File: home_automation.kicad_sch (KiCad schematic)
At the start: 44 parts

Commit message: Anotate the Components
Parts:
- gave numbers to parts that had none: 44

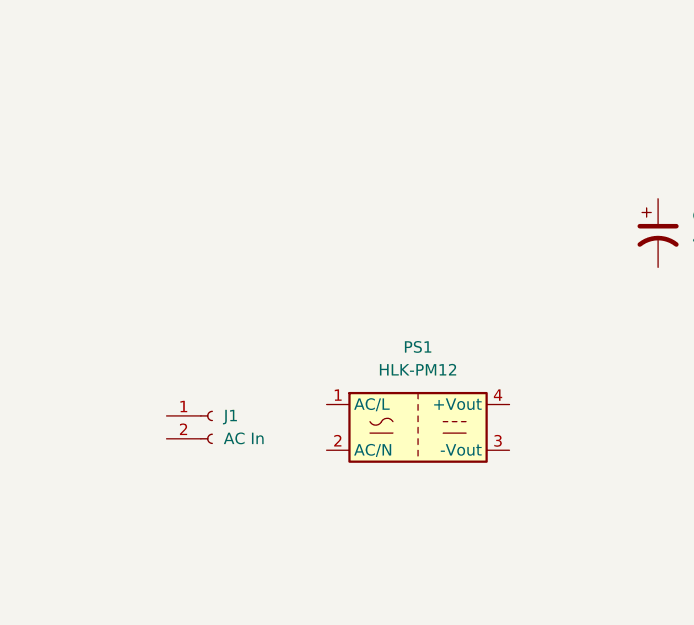
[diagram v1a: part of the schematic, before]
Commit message: Power section Wiring Completed
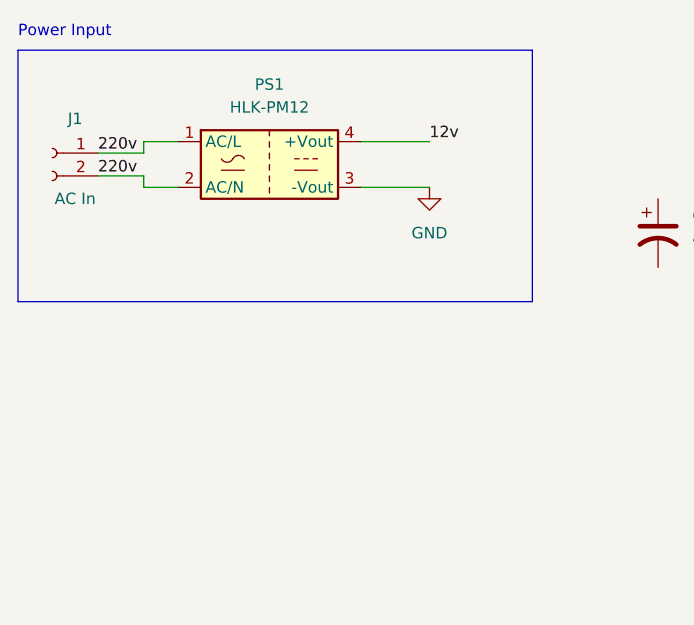
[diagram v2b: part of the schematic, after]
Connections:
- net 220v: now reaches J1.1 (Pin_1)
- net 220v: now also J1.2 (Pin_2), PS1.1 (AC/L), PS1.2 (AC/N)
- net GND: now reaches PS1.3 (-Vout)
- net 12v: now reaches PS1.4 (+Vout)
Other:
- note added: "Power Input"
- moved on the sheet: J1, PS1
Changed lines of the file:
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@@
     (rev "v1")
+  )
+  (wire (pts (xy 34.29 29.21) (xy 39.37 29.21))
+    (stroke (width 0) (type default) (color 0 0 0 0))
+  )
+  (wire (pts (xy 39.37 27.94) (xy 43.18 27.94))
+    (stroke (width 0) (type default) (color 0 0 0 0))
+  )
+  (wire (pts (xy 39.37 31.75) (xy 39.37 33.02))
+    (stroke (width 0) (type default) (color 0 0 0 0))
+  )
+  (polyline (pts (xy 25.4 17.78) (xy 82.55 17.78))
+    (stroke (width 0) (type default) (color 0 0 0 0))
+  )
+  (wire (pts (xy 63.5 33.02) (xy 71.12 33.02))
+    (stroke (width 0) (type default) (color 0 0 0 0))
+  )
+  (wire (pts (xy 63.5 27.94) (xy 71.12 27.94))
+    (stroke (width 0) (type default) (color 0 0 0 0))
+  )
+  (polyline (pts (xy 25.4 17.78) (xy 25.4 45.72))
+    (stroke (width 0) (type default) (color 0 0 0 0))
+  )
+  (polyline (pts (xy 82.55 45.72) (xy 25.4 45.72))
+    (stroke (width 0) (type default) (color 0 0 0 0))
+  )
+  (wire (pts (xy 34.29 31.75) (xy 39.37 31.75))
+    (stroke (width 0) (type default) (color 0 0 0 0))
+  )
+  (polyline (pts (xy 82.55 17.78) (xy 82.55 45.72))
+    (stroke (width 0) (type default) (color 0 0 0 0))
+  )
+  (wire (pts (xy 39.37 33.02) (xy 43.18 33.02))
+    (stroke (width 0) (type default) (color 0 0 0 0))
+  )
+  (wire (pts (xy 39.37 29.21) (xy 39.37 27.94))
+    (stroke (width 0) (type default) (color 0 0 0 0))
+  )
+  (text "Power Input\n" (at 25.4 16.51 0)
+    (effects (font (size 1.27 1.27)) (justify left bottom))
+  )
+  (label "12v" (at 71.12 27.94 0)
+    (effects (font (size 1.27 1.27)) (justify left bottom))
+  )
+  (label "220v" (at 34.29 29.21 0)
+    (effects (font (size 1.27 1.27)) (justify left bottom))
+  )
+  (label "220v" (at 34.29 31.75 0)
+    (effects (font (size 1.27 1.27)) (justify left bottom))
   )
   (symbol (lib_id "Transistor_CUSTOM:D882_NPN_transistor") (at 245.11 149.86 0) (unit 1)
@@
     (pin "2")
   )
+  (symbol (lib_id "power:GND") (at 71.12 33.02 0) (unit 1)
+    (in_bom yes) (on_board yes) (fields_autoplaced)
+    (property "Reference" "#PWR?" (id 0) (at 71.12 39.37 0)
+      (effects (font (size 1.27 1.27)) hide)
+    )
+    (property "Value" "GND" (id 1) (at 71.12 38.1 0))
+    (property "Footprint" "" (id 2) (at 71.12 33.02 0)
+      (effects (font (size 1.27 1.27)) hide)
+    )
+    (property "Datasheet" "" (id 3) (at 71.12 33.02 0)
+      (effects (font (size 1.27 1.27)) hide)
+    )
+    (pin "1")
+  )
   (symbol (lib_id "Relay_SPDT:Relay_SPDT") (at 127 142.24 0) (unit 1)
     (in_bom yes) (on_board yes) (fields_autoplaced)
@@
     (pin "4")
   )
-  (symbol (lib_id "Connector:Conn_01x02_Female") (at 46.99 58.42 0) (unit 1)
-    (in_bom yes) (on_board yes) (fields_autoplaced)
-    (property "Reference" "J1" (id 0) (at 48.26 58.4199 0)
-      (effects (font (size 1.27 1.27)) (justify left))
-    )
-    (property "Value" "AC In" (id 1) (at 48.26 60.9599 0)
-      (effects (font (size 1.27 1.27)) (justify left))
-    )
-    (property "Footprint" "" (id 2) (at 46.99 58.42 0)
-      (effects (font (size 1.27 1.27)) hide)
-    )
-    (property "Datasheet" "~" (id 3) (at 46.99 58.42 0)
+  (symbol (lib_id "Connector:Conn_01x02_Female") (at 29.21 29.21 0) (mirror y) (unit 1)
+    (in_bom yes) (on_board yes)
+    (property "Reference" "J1" (id 0) (at 31.75 25.4 0))
+    (property "Value" "AC In" (id 1) (at 31.75 34.29 0))
+    (property "Footprint" "" (id 2) (at 29.21 29.21 0)
+      (effects (font (size 1.27 1.27)) hide)
+    )
+    (property "Datasheet" "~" (id 3) (at 29.21 29.21 0)
       (effects (font (size 1.27 1.27)) hide)
     )
@@
     (pin "2")
   )
-  (symbol (lib_id "Converter_ACDC:HLK-PM12") (at 69.85 59.69 0) (unit 1)
-    (in_bom yes) (on_board yes) (fields_autoplaced)
-    (property "Reference" "PS1" (id 0) (at 69.85 50.8 0))
-    (property "Value" "HLK-PM12" (id 1) (at 69.85 53.34 0))
-    (property "Footprint" "Converter_ACDC:Converter_ACDC_HiLink_HLK-PMxx" (id 2) (at 69.85 67.31 0)
-      (effects (font (size 1.27 1.27)) hide)
-    )
-    (property "Datasheet" "http://www.hlktech.net/product_detail.php?ProId=56" (id 3) (at 80.01 68.58 0)
+  (symbol (lib_id "Converter_ACDC:HLK-PM12") (at 53.34 30.48 0) (unit 1)
+    (in_bom yes) (on_board yes) (fields_autoplaced)
+    (property "Reference" "PS1" (id 0) (at 53.34 21.59 0))
+    (property "Value" "HLK-PM12" (id 1) (at 53.34 24.13 0))
+    (property "Footprint" "Converter_ACDC:Converter_ACDC_HiLink_HLK-PMxx" (id 2) (at 53.34 38.1 0)
+      (effects (font (size 1.27 1.27)) hide)
+    )
+    (property "Datasheet" "http://www.hlktech.net/product_detail.php?ProId=56" (id 3) (at 63.5 39.37 0)
       (effects (font (size 1.27 1.27)) hide)
     )
@@
   )
   (symbol_instances
+    (path "/2accfbf2-56a4-48cd-9686-a76d5e02c6cd"
+      (reference "#PWR?") (unit 1) (value "GND") (footprint "")
+    )
     (path "/6bde53ab-782b-4476-8581-8063e3f079ec"
       (reference "C1") (unit 1) (value "470uF") (footprint "")

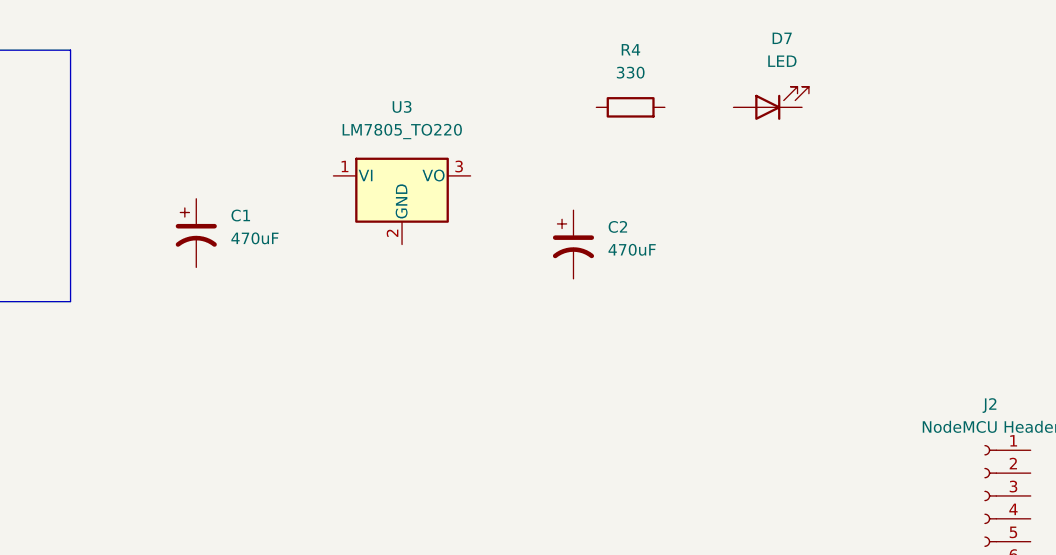
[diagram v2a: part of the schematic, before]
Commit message: 12v to 5v  Wiring Completed
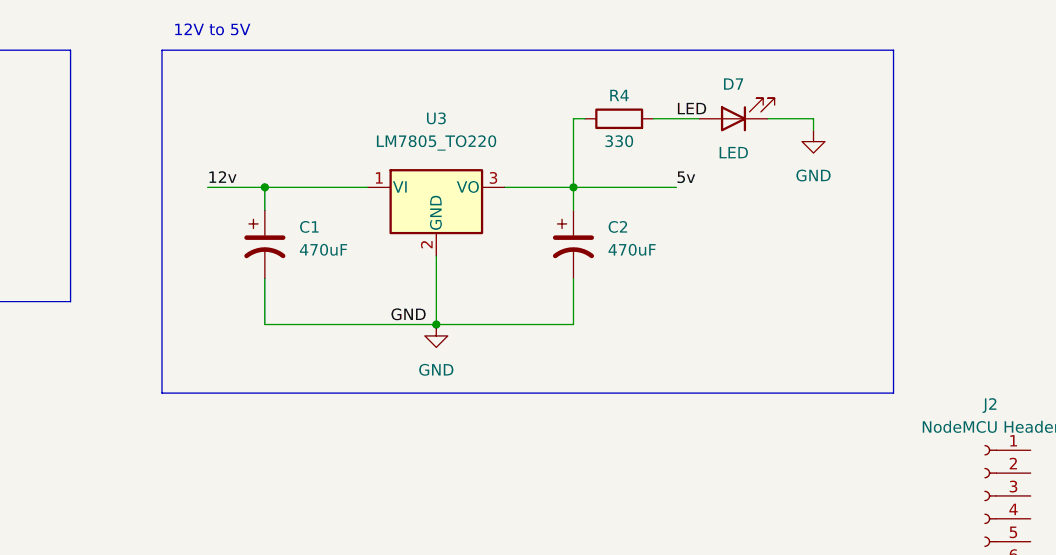
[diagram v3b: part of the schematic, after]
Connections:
- net 12v: now also C1.1, U3.1 (VI)
- net GND: now also C1.2, C2.2, D7.1 (K), U3.2 (GND)
- net 5v: now reaches C2.1
- net 5v: now also R4.1, U3.3 (VO)
- net LED: now reaches D7.2 (A)
- net LED: now also R4.2
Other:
- note added: "12V to 5V"
- moved on the sheet: C1, D7, R4, U3
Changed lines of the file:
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@@
     (rev "v1")
   )
+  (junction (at 104.14 33.02) (diameter 0) (color 0 0 0 0)
+  )
+  (junction (at 138.43 33.02) (diameter 0) (color 0 0 0 0)
+  )
+  (junction (at 123.19 48.26) (diameter 0) (color 0 0 0 0)
+  )
+  (wire (pts (xy 123.19 48.26) (xy 138.43 48.26))
+    (stroke (width 0) (type default) (color 0 0 0 0))
+  )
+  (wire (pts (xy 138.43 33.02) (xy 138.43 35.56))
+    (stroke (width 0) (type default) (color 0 0 0 0))
+  )
+  (wire (pts (xy 104.14 33.02) (xy 115.57 33.02))
+    (stroke (width 0) (type default) (color 0 0 0 0))
+  )
   (wire (pts (xy 34.29 29.21) (xy 39.37 29.21))
     (stroke (width 0) (type default) (color 0 0 0 0))
   )
+  (polyline (pts (xy 173.99 55.88) (xy 92.71 55.88))
+    (stroke (width 0) (type default) (color 0 0 0 0))
+  )
   (wire (pts (xy 39.37 27.94) (xy 43.18 27.94))
     (stroke (width 0) (type default) (color 0 0 0 0))
   )
+  (wire (pts (xy 147.32 25.4) (xy 152.4 25.4))
+    (stroke (width 0) (type default) (color 0 0 0 0))
+  )
+  (polyline (pts (xy 92.71 17.78) (xy 92.71 55.88))
+    (stroke (width 0) (type default) (color 0 0 0 0))
+  )
+  (wire (pts (xy 139.7 25.4) (xy 138.43 25.4))
+    (stroke (width 0) (type default) (color 0 0 0 0))
+  )
   (wire (pts (xy 39.37 31.75) (xy 39.37 33.02))
     (stroke (width 0) (type default) (color 0 0 0 0))
   )
+  (wire (pts (xy 130.81 33.02) (xy 138.43 33.02))
+    (stroke (width 0) (type default) (color 0 0 0 0))
+  )
+  (wire (pts (xy 138.43 25.4) (xy 138.43 33.02))
+    (stroke (width 0) (type default) (color 0 0 0 0))
+  )
+  (wire (pts (xy 123.19 40.64) (xy 123.19 48.26))
+    (stroke (width 0) (type default) (color 0 0 0 0))
+  )
+  (wire (pts (xy 138.43 33.02) (xy 149.86 33.02))
+    (stroke (width 0) (type default) (color 0 0 0 0))
+  )
   (polyline (pts (xy 25.4 17.78) (xy 82.55 17.78))
     (stroke (width 0) (type default) (color 0 0 0 0))
@@
     (stroke (width 0) (type default) (color 0 0 0 0))
   )
+  (wire (pts (xy 138.43 48.26) (xy 138.43 43.18))
+    (stroke (width 0) (type default) (color 0 0 0 0))
+  )
+  (wire (pts (xy 104.14 43.18) (xy 104.14 48.26))
+    (stroke (width 0) (type default) (color 0 0 0 0))
+  )
   (wire (pts (xy 63.5 27.94) (xy 71.12 27.94))
     (stroke (width 0) (type default) (color 0 0 0 0))
   )
+  (polyline (pts (xy 92.71 17.78) (xy 173.99 17.78))
+    (stroke (width 0) (type default) (color 0 0 0 0))
+  )
   (polyline (pts (xy 25.4 17.78) (xy 25.4 45.72))
     (stroke (width 0) (type default) (color 0 0 0 0))
   )
+  (wire (pts (xy 165.1 25.4) (xy 165.1 26.67))
+    (stroke (width 0) (type default) (color 0 0 0 0))
+  )
+  (wire (pts (xy 97.79 33.02) (xy 104.14 33.02))
+    (stroke (width 0) (type default) (color 0 0 0 0))
+  )
   (polyline (pts (xy 82.55 45.72) (xy 25.4 45.72))
     (stroke (width 0) (type default) (color 0 0 0 0))
@@
     (stroke (width 0) (type default) (color 0 0 0 0))
   )
+  (polyline (pts (xy 173.99 17.78) (xy 173.99 55.88))
+    (stroke (width 0) (type default) (color 0 0 0 0))
+  )
   (polyline (pts (xy 82.55 17.78) (xy 82.55 45.72))
     (stroke (width 0) (type default) (color 0 0 0 0))
   )
+  (wire (pts (xy 160.02 25.4) (xy 165.1 25.4))
+    (stroke (width 0) (type default) (color 0 0 0 0))
+  )
   (wire (pts (xy 39.37 33.02) (xy 43.18 33.02))
+    (stroke (width 0) (type default) (color 0 0 0 0))
+  )
+  (wire (pts (xy 104.14 33.02) (xy 104.14 35.56))
+    (stroke (width 0) (type default) (color 0 0 0 0))
+  )
+  (wire (pts (xy 104.14 48.26) (xy 123.19 48.26))
     (stroke (width 0) (type default) (color 0 0 0 0))
   )
@@
     (effects (font (size 1.27 1.27)) (justify left bottom))
   )
+  (text "12V to 5V\n" (at 93.98 16.51 0)
+    (effects (font (size 1.27 1.27)) (justify left bottom))
+  )
   (label "12v" (at 71.12 27.94 0)
     (effects (font (size 1.27 1.27)) (justify left bottom))
@@
     (effects (font (size 1.27 1.27)) (justify left bottom))
   )
+  (label "GND" (at 118.11 48.26 0)
+    (effects (font (size 1.27 1.27)) (justify left bottom))
+  )
   (label "220v" (at 34.29 31.75 0)
+    (effects (font (size 1.27 1.27)) (justify left bottom))
+  )
+  (label "5v" (at 149.86 33.02 0)
+    (effects (font (size 1.27 1.27)) (justify left bottom))
+  )
+  (label "LED" (at 149.86 25.4 0)
+    (effects (font (size 1.27 1.27)) (justify left bottom))
+  )
+  (label "12v" (at 97.79 33.02 0)
     (effects (font (size 1.27 1.27)) (justify left bottom))
   )
@@
     (pin "3")
   )
-  (symbol (lib_id "Regulator_Linear:LM7805_TO220") (at 119.38 31.75 0) (unit 1)
-    (in_bom yes) (on_board yes) (fields_autoplaced)
-    (property "Reference" "U3" (id 0) (at 119.38 24.13 0))
-    (property "Value" "LM7805_TO220" (id 1) (at 119.38 26.67 0))
-    (property "Footprint" "Package_TO_SOT_THT:TO-220-3_Vertical" (id 2) (at 119.38 26.035 0)
+  (symbol (lib_id "Regulator_Linear:LM7805_TO220") (at 123.19 33.02 0) (unit 1)
+    (in_bom yes) (on_board yes) (fields_autoplaced)
+    (property "Reference" "U3" (id 0) (at 123.19 25.4 0))
+    (property "Value" "LM7805_TO220" (id 1) (at 123.19 27.94 0))
+    (property "Footprint" "Package_TO_SOT_THT:TO-220-3_Vertical" (id 2) (at 123.19 27.305 0)
       (effects (font (size 1.27 1.27) italic) hide)
     )
-    (property "Datasheet" "https://www.onsemi.cn/PowerSolutions/document/MC7800-D.PDF" (id 3) (at 119.38 33.02 0)
+    (property "Datasheet" "https://www.onsemi.cn/PowerSolutions/document/MC7800-D.PDF" (id 3) (at 123.19 34.29 0)
       (effects (font (size 1.27 1.27)) hide)
     )
@@
     (pin "3")
     (pin "4")
+  )
+  (symbol (lib_id "power:GND") (at 123.19 48.26 0) (unit 1)
+    (in_bom yes) (on_board yes) (fields_autoplaced)
+    (property "Reference" "#PWR?" (id 0) (at 123.19 54.61 0)
+      (effects (font (size 1.27 1.27)) hide)
+    )
+    (property "Value" "GND" (id 1) (at 123.19 53.34 0))
+    (property "Footprint" "" (id 2) (at 123.19 48.26 0)
+      (effects (font (size 1.27 1.27)) hide)
+    )
+    (property "Datasheet" "" (id 3) (at 123.19 48.26 0)
+      (effects (font (size 1.27 1.27)) hide)
+    )
+    (pin "1")
   )
   (symbol (lib_id "Connector:Conn_01x02_Female") (at 29.21 29.21 0) (mirror y) (unit 1)
@@
     (pin "2")
   )
-  (symbol (lib_id "Device:LED") (at 160.02 24.13 180) (unit 1)
-    (in_bom yes) (on_board yes) (fields_autoplaced)
-    (property "Reference" "D7" (id 0) (at 161.6075 16.51 0))
-    (property "Value" "LED" (id 1) (at 161.6075 19.05 0))
-    (property "Footprint" "" (id 2) (at 160.02 24.13 0)
-      (effects (font (size 1.27 1.27)) hide)
-    )
-    (property "Datasheet" "~" (id 3) (at 160.02 24.13 0)
+  (symbol (lib_id "Device:LED") (at 156.21 25.4 180) (unit 1)
+    (in_bom yes) (on_board yes)
+    (property "Reference" "D7" (id 0) (at 156.21 21.59 0))
+    (property "Value" "LED" (id 1) (at 156.21 29.21 0))
+    (property "Footprint" "" (id 2) (at 156.21 25.4 0)
+      (effects (font (size 1.27 1.27)) hide)
+    )
+    (property "Datasheet" "~" (id 3) (at 156.21 25.4 0)
       (effects (font (size 1.27 1.27)) hide)
     )
@@
     (pin "3")
   )
-  (symbol (lib_id "Device:C_Polarized_US") (at 96.52 38.1 0) (unit 1)
-    (in_bom yes) (on_board yes) (fields_autoplaced)
-    (property "Reference" "C1" (id 0) (at 100.33 36.1949 0)
-      (effects (font (size 1.27 1.27)) (justify left))
-    )
-    (property "Value" "470uF" (id 1) (at 100.33 38.7349 0)
-      (effects (font (size 1.27 1.27)) (justify left))
-    )
-    (property "Footprint" "" (id 2) (at 96.52 38.1 0)
-      (effects (font (size 1.27 1.27)) hide)
-    )
-    (property "Datasheet" "~" (id 3) (at 96.52 38.1 0)
+  (symbol (lib_id "Device:C_Polarized_US") (at 104.14 39.37 0) (unit 1)
+    (in_bom yes) (on_board yes) (fields_autoplaced)
+    (property "Reference" "C1" (id 0) (at 107.95 37.4649 0)
+      (effects (font (size 1.27 1.27)) (justify left))
+    )
+    (property "Value" "470uF" (id 1) (at 107.95 40.0049 0)
+      (effects (font (size 1.27 1.27)) (justify left))
+    )
+    (property "Footprint" "" (id 2) (at 104.14 39.37 0)
+      (effects (font (size 1.27 1.27)) hide)
+    )
+    (property "Datasheet" "~" (id 3) (at 104.14 39.37 0)
       (effects (font (size 1.27 1.27)) hide)
     )
@@
     (pin "9")
   )
-  (symbol (lib_id "Device:R") (at 144.78 24.13 90) (unit 1)
-    (in_bom yes) (on_board yes) (fields_autoplaced)
-    (property "Reference" "R4" (id 0) (at 144.78 17.78 90))
-    (property "Value" "330" (id 1) (at 144.78 20.32 90))
-    (property "Footprint" "" (id 2) (at 144.78 25.908 90)
-      (effects (font (size 1.27 1.27)) hide)
-    )
-    (property "Datasheet" "~" (id 3) (at 144.78 24.13 0)
+  (symbol (lib_id "Device:R") (at 143.51 25.4 90) (unit 1)
+    (in_bom yes) (on_board yes)
+    (property "Reference" "R4" (id 0) (at 143.51 22.86 90))
+    (property "Value" "330" (id 1) (at 143.51 27.94 90))
+    (property "Footprint" "" (id 2) (at 143.51 27.178 90)
+      (effects (font (size 1.27 1.27)) hide)
+    )
+    (property "Datasheet" "~" (id 3) (at 143.51 25.4 0)
       (effects (font (size 1.27 1.27)) hide)
     )
@@
     (pin "1")
     (pin "2")
+  )
+  (symbol (lib_id "power:GND") (at 165.1 26.67 0) (unit 1)
+    (in_bom yes) (on_board yes) (fields_autoplaced)
+    (property "Reference" "#PWR?" (id 0) (at 165.1 33.02 0)
+      (effects (font (size 1.27 1.27)) hide)
+    )
+    (property "Value" "GND" (id 1) (at 165.1 31.75 0))
+    (property "Footprint" "" (id 2) (at 165.1 26.67 0)
+      (effects (font (size 1.27 1.27)) hide)
+    )
+    (property "Datasheet" "" (id 3) (at 165.1 26.67 0)
+      (effects (font (size 1.27 1.27)) hide)
+    )
+    (pin "1")
   )
   (symbol (lib_id "Device:R") (at 166.37 189.23 0) (unit 1)
@@
       (reference "#PWR?") (unit 1) (value "GND") (footprint "")
     )
+    (path "/5f3cabc5-f5f9-4867-bd79-bd61a730f705"
+      (reference "#PWR?") (unit 1) (value "GND") (footprint "")
+    )
+    (path "/7ee91c53-61a7-455e-afd3-92379e1ab5c7"
+      (reference "#PWR?") (unit 1) (value "GND") (footprint "")
+    )
